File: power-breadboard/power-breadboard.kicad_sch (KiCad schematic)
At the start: 0 parts

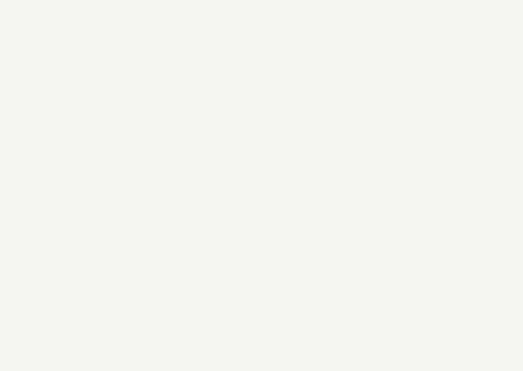
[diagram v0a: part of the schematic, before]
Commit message: power-breadboard: complete non-iso. interfaces
- CAN transceiver
- Power input (battery and 24V->5V converter)
- MEBC telemetry power connector
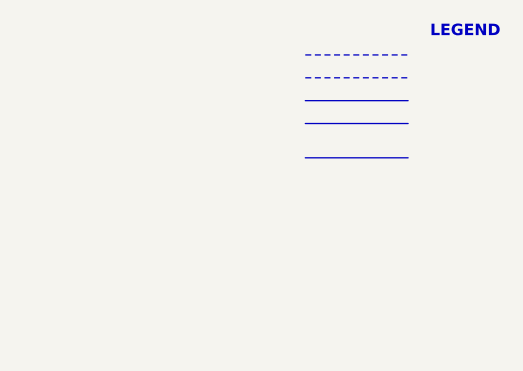
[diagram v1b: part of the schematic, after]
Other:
- note added: "LEGEND"

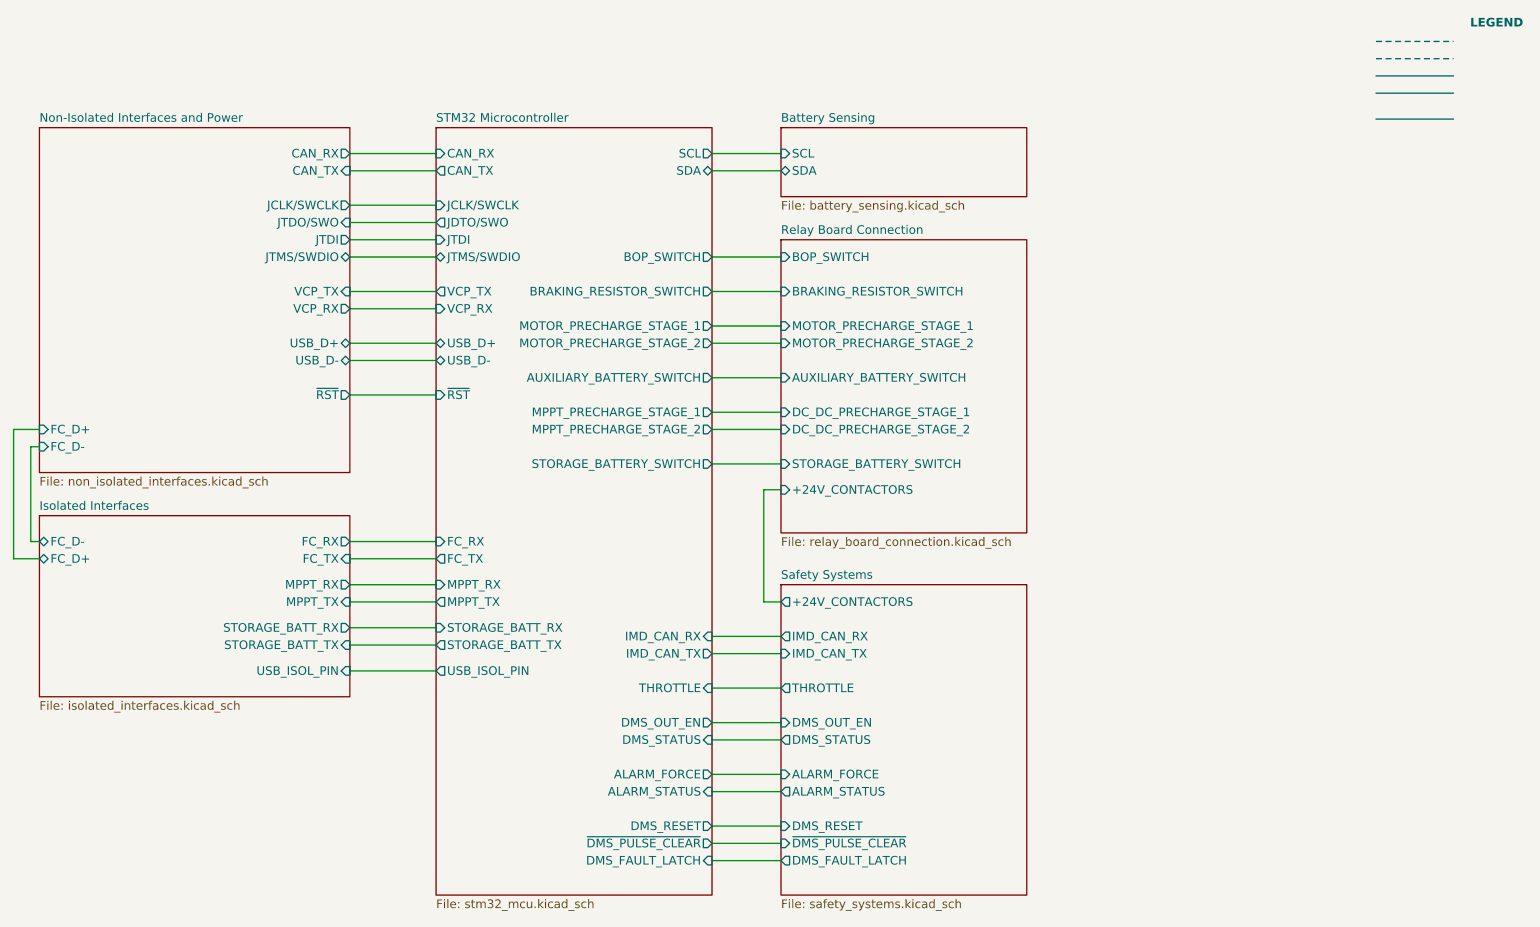
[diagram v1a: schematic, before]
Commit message: power-breadboard: rename stm32 sheet to nucleo
Also removed unused sheet pins on main page.
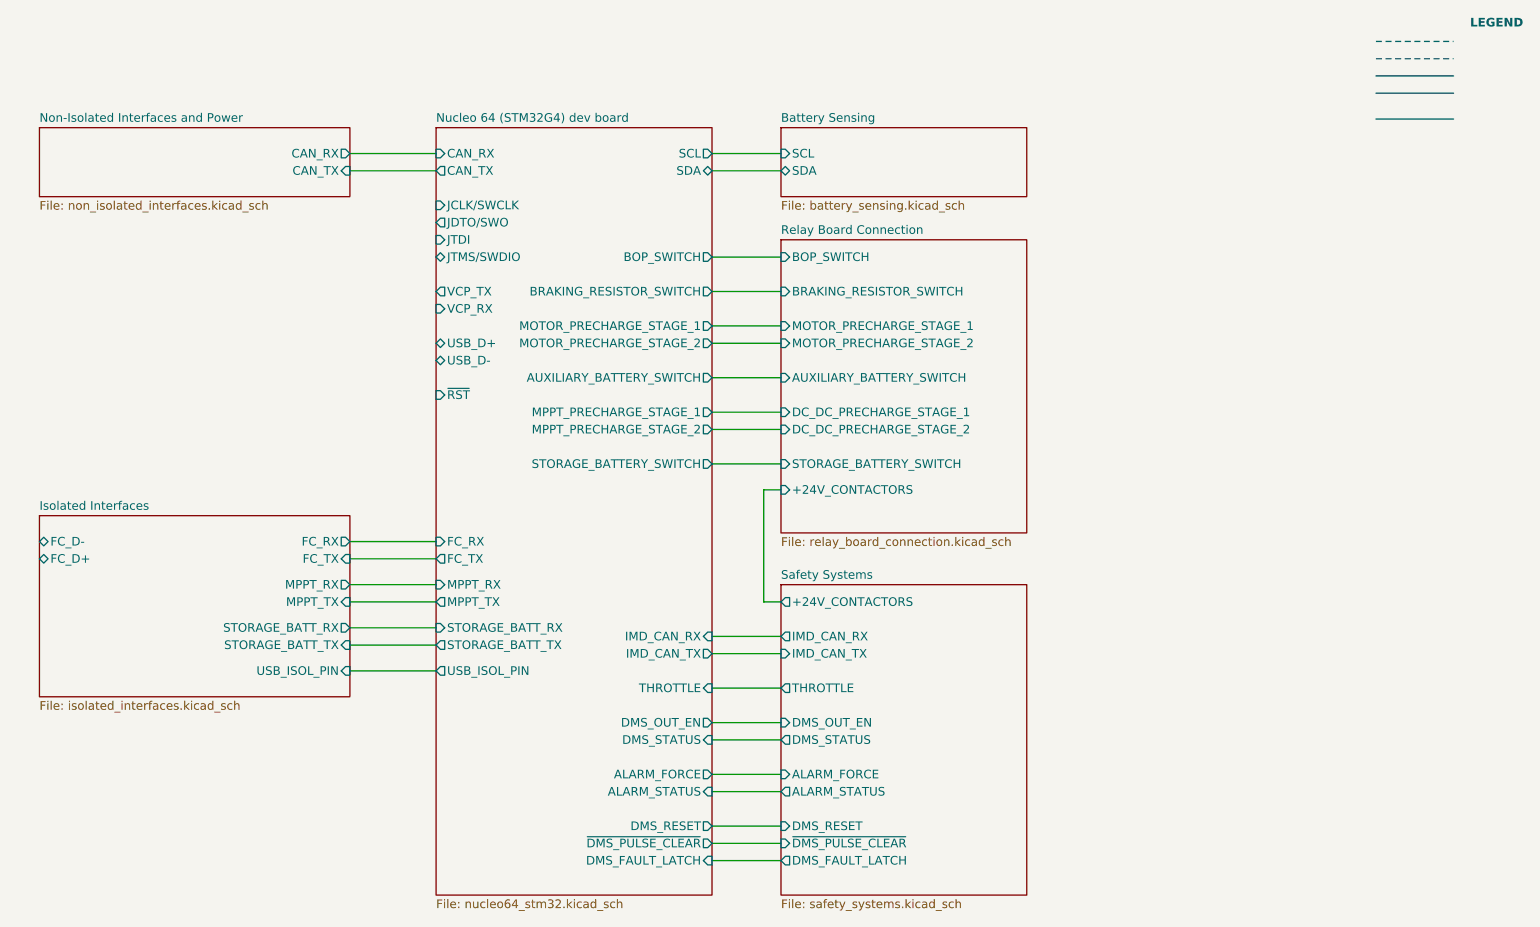
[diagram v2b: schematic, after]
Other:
- sheet STM32 Microcontroller renamed Nucleo 64 (STM32G4) dev board
- sheet Non-Isolated Interfaces and Power ports: added none; removed FC_D+, FC_D-, JCLK/SWCLK, JTDI, JTDO/SWO, JTMS/SWDIO, USB_D+, USB_D-, VCP_RX, VCP_TX, ~{RST}
- sheet Nucleo 64 (STM32G4) dev board: file stm32_mcu.kicad_sch -> nucleo64_stm32.kicad_sch

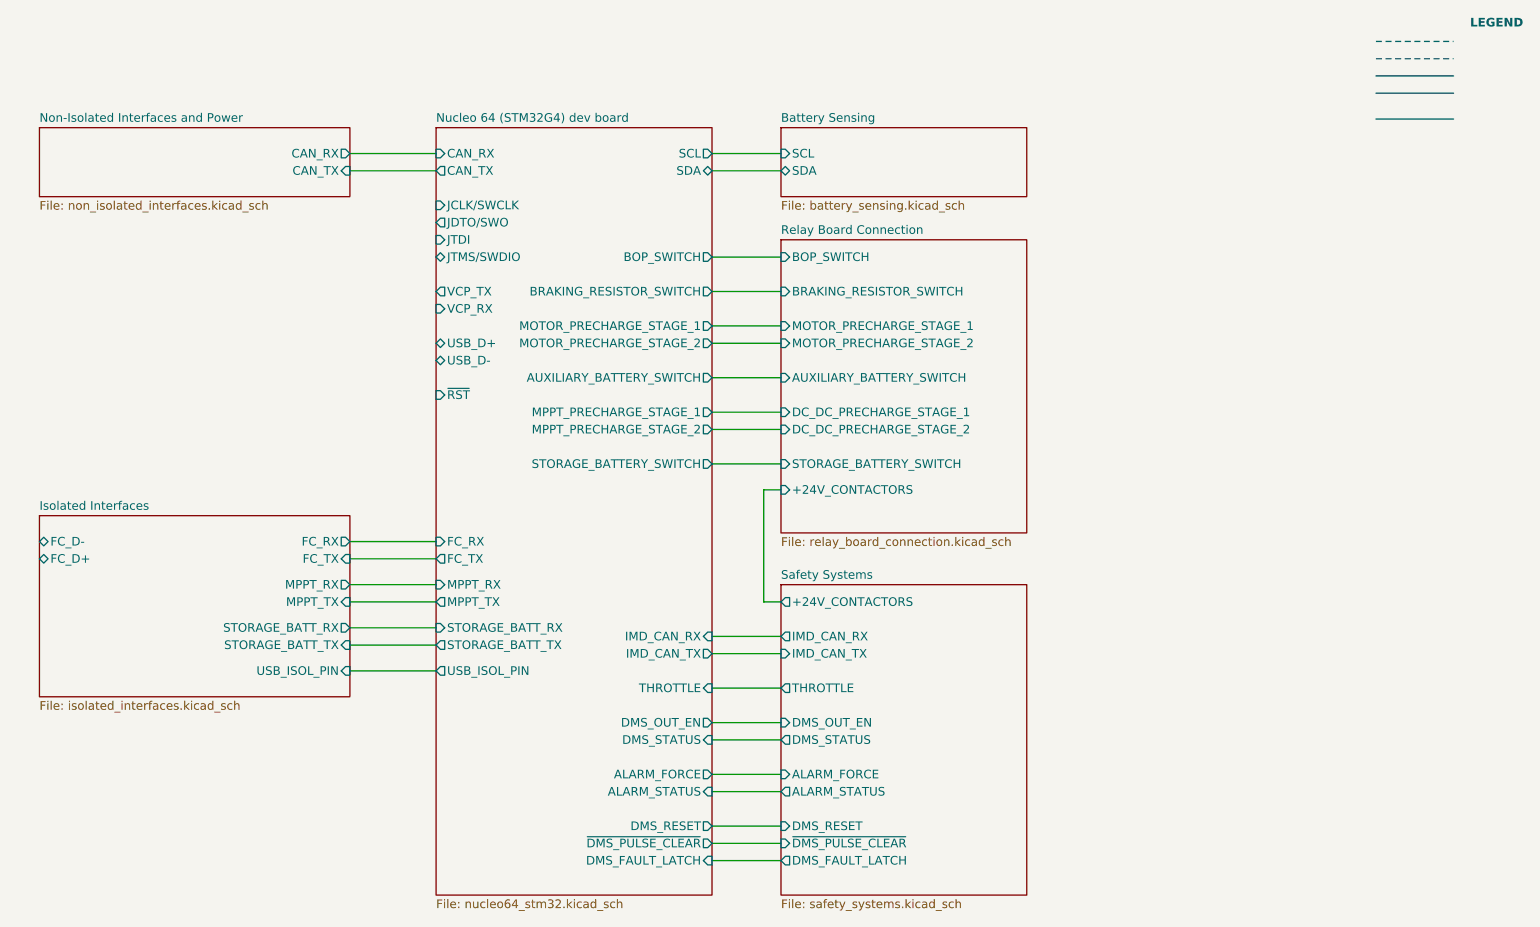
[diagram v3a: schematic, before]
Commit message: power-breadboard: rename relay-board page
There are now multiple relay boards.

Also cleaned up some sheet pins on the main page.
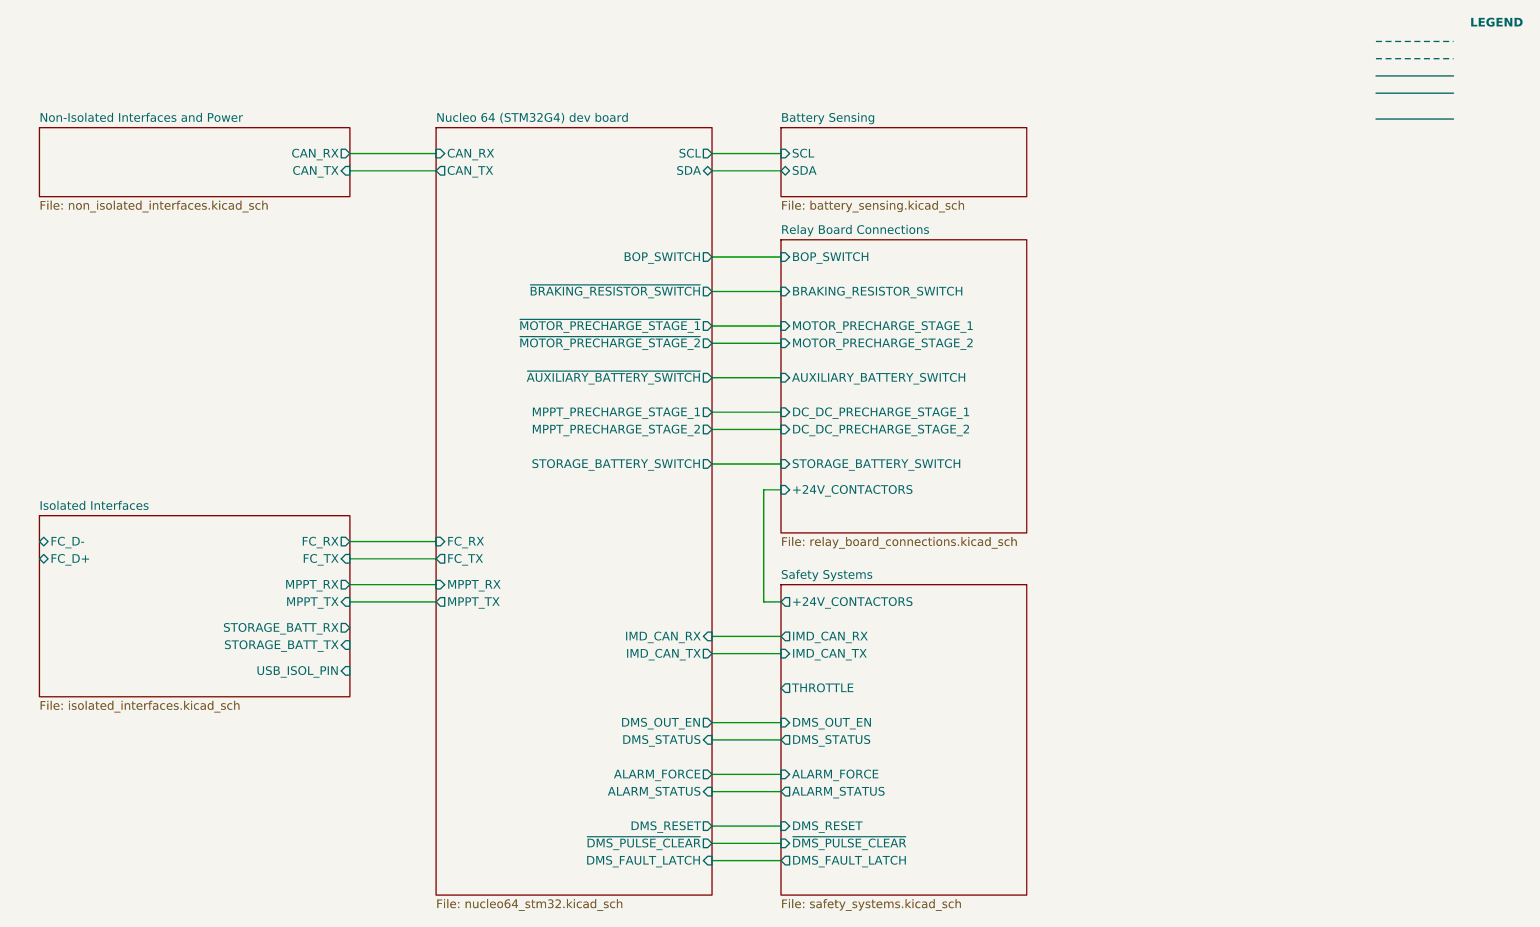
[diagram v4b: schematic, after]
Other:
- sheet Relay Board Connection renamed Relay Board Connections
- sheet Nucleo 64 (STM32G4) dev board ports: added ~{AUXILIARY_BATTERY_SWITCH}, ~{BRAKING_RESISTOR_SWITCH}, ~{MOTOR_PRECHARGE_STAGE_1}, ~{MOTOR_PRECHARGE_STAGE_2}; removed AUXILIARY_BATTERY_SWITCH, BRAKING_RESISTOR_SWITCH, JCLK/SWCLK, JDTO/SWO, JTDI, JTMS/SWDIO, MOTOR_PRECHARGE_STAGE_1, MOTOR_PRECHARGE_STAGE_2, STORAGE_BATT_RX, STORAGE_BATT_TX, THROTTLE, USB_D+, USB_D-, USB_ISOL_PIN, VCP_RX, VCP_TX, ~{RST}
- sheet Relay Board Connections: file relay_board_connection.kicad_sch -> relay_board_connections.kicad_sch
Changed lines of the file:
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@@
-	(wire
-		(pts
-			(xy 93.98 110.49) (xy 106.68 110.49)
-		)
-		(stroke
-			(width 0)
-			(type default)
-		)
-	)
-	(wire
-		(pts
-			(xy 93.98 104.14) (xy 106.68 104.14)
-		)
-		(stroke
-			(width 0)
-			(type default)
-		)
-	)
 	(wire
 		(pts
@@
 		)
 	)
-	(wire
-		(pts
-			(xy 147.32 113.03) (xy 157.48 113.03)
-		)
-		(stroke
-			(width 0)
-			(type default)
-		)
-	)
 	(polyline
 		(pts
@@
 		(pts
 			(xy 147.32 107.95) (xy 157.48 107.95)
-		)
-		(stroke
-			(width 0)
-			(type default)
-		)
-	)
-	(wire
-		(pts
-			(xy 93.98 106.68) (xy 106.68 106.68)
 		)
 		(stroke
@@
 			)
 		)
-		(pin "JCLK{slash}SWCLK" input
-			(at 106.68 41.91 180)
-			(effects
-				(font
-					(size 1.27 1.27)
-				)
-				(justify left)
-			)
-		)
-		(pin "JDTO{slash}SWO" output
-			(at 106.68 44.45 180)
-			(effects
-				(font
-					(size 1.27 1.27)
-				)
-				(justify left)
-			)
-		)
-		(pin "JTDI" input
-			(at 106.68 46.99 180)
-			(effects
-				(font
-					(size 1.27 1.27)
-				)
-				(justify left)
-			)
-		)
-		(pin "JTMS{slash}SWDIO" bidirectional
-			(at 106.68 49.53 180)
-			(effects
-				(font
-					(size 1.27 1.27)
-				)
-				(justify left)
-			)
-		)
 		(pin "SCL" output
 			(at 147.32 34.29 0)
@@
 			)
 		)
-		(pin "USB_D+" bidirectional
-			(at 106.68 62.23 180)
-			(effects
-				(font
-					(size 1.27 1.27)
-				)
-				(justify left)
-			)
-		)
-		(pin "USB_D-" bidirectional
-			(at 106.68 64.77 180)
-			(effects
-				(font
-					(size 1.27 1.27)
-				)
-				(justify left)
-			)
-		)
-		(pin "VCP_RX" input
-			(at 106.68 57.15 180)
-			(effects
-				(font
-					(size 1.27 1.27)
-				)
-				(justify left)
-			)
-		)
-		(pin "VCP_TX" output
-			(at 106.68 54.61 180)
-			(effects
-				(font
-					(size 1.27 1.27)
-				)
-				(justify left)
-			)
-		)
-		(pin "~{RST}" input
-			(at 106.68 69.85 180)
-			(effects
-				(font
-					(size 1.27 1.27)
-				)
-				(justify left)
-			)
-		)
 		(pin "ALARM_FORCE" output
 			(at 147.32 125.73 0)
@@
 			)
 		)
-		(pin "AUXILIARY_BATTERY_SWITCH" output
-			(at 147.32 67.31 0)
-			(effects
-				(font
-					(size 1.27 1.27)
-				)
-				(justify right)
-			)
-		)
 		(pin "BOP_SWITCH" output
 			(at 147.32 49.53 0)
@@
 			)
 		)
-		(pin "BRAKING_RESISTOR_SWITCH" output
-			(at 147.32 54.61 0)
-			(effects
-				(font
-					(size 1.27 1.27)
-				)
-				(justify right)
-			)
-		)
 		(pin "DMS_STATUS" input
 			(at 147.32 120.65 0)
@@
 			)
 		)
-		(pin "MOTOR_PRECHARGE_STAGE_1" output
-			(at 147.32 59.69 0)
-			(effects
-				(font
-					(size 1.27 1.27)
-				)
-				(justify right)
-			)
-		)
-		(pin "MOTOR_PRECHARGE_STAGE_2" output
-			(at 147.32 62.23 0)
-			(effects
-				(font
-					(size 1.27 1.27)
-				)
-				(justify right)
-			)
-		)
 		(pin "MPPT_PRECHARGE_STAGE_1" output
 			(at 147.32 72.39 0)
@@
 			)
 		)
-		(pin "THROTTLE" input
-			(at 147.32 113.03 0)
-			(effects
-				(font
-					(size 1.27 1.27)
-				)
-				(justify right)
-			)
-		)
-		(pin "USB_ISOL_PIN" output
-			(at 106.68 110.49 180)
-			(effects
-				(font
-					(size 1.27 1.27)
-				)
-				(justify left)
-			)
-		)
 		(pin "DMS_OUT_EN" output
 			(at 147.32 118.11 0)
@@
 			)
 		)
-		(pin "STORAGE_BATT_RX" input
-			(at 106.68 104.14 180)
-			(effects
-				(font
-					(size 1.27 1.27)
-				)
-				(justify left)
-			)
-		)
-		(pin "STORAGE_BATT_TX" output
-			(at 106.68 106.68 180)
-			(effects
-				(font
-					(size 1.27 1.27)
-				)
-				(justify left)
-			)
-		)
 		(pin "DMS_RESET" output
 			(at 147.32 133.35 0)
@@
 		(pin "DMS_FAULT_LATCH" input
 			(at 147.32 138.43 0)
+			(effects
+				(font
+					(size 1.27 1.27)
+				)
+				(justify right)
+			)
+		)
+		(pin "~{AUXILIARY_BATTERY_SWITCH}" output
+			(at 147.32 67.31 0)
+			(effects
+				(font
+					(size 1.27 1.27)
+				)
+				(justify right)
+			)
+		)
+		(pin "~{BRAKING_RESISTOR_SWITCH}" output
+			(at 147.32 54.61 0)
+			(effects
+				(font
+					(size 1.27 1.27)
+				)
+				(justify right)
+			)
+		)
+		(pin "~{MOTOR_PRECHARGE_STAGE_1}" output
+			(at 147.32 59.69 0)
+			(effects
+				(font
+					(size 1.27 1.27)
+				)
+				(justify right)
+			)
+		)
+		(pin "~{MOTOR_PRECHARGE_STAGE_2}" output
+			(at 147.32 62.23 0)
 			(effects
 				(font
@@
 			(color 0 0 0 0)
 		)
-		(property "Sheetname" "Relay Board Connection"
+		(property "Sheetname" "Relay Board Connections"
 			(at 157.48 46.2784 0)
 			(show_name no)
@@
 			)
 		)
-		(property "Sheetfile" "relay_board_connection.kicad_sch"
+		(property "Sheetfile" "relay_board_connections.kicad_sch"
 			(at 157.48 90.7546 0)
 			(show_name no)
